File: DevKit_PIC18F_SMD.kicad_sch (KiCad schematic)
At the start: 25 parts, among them J1 PIC_ICSP_ICD, J2 USB_B_Mini, J5 RIGHT_PORT, J6 LEFT_PORT, SW1 SW_RST, X1 16MHz

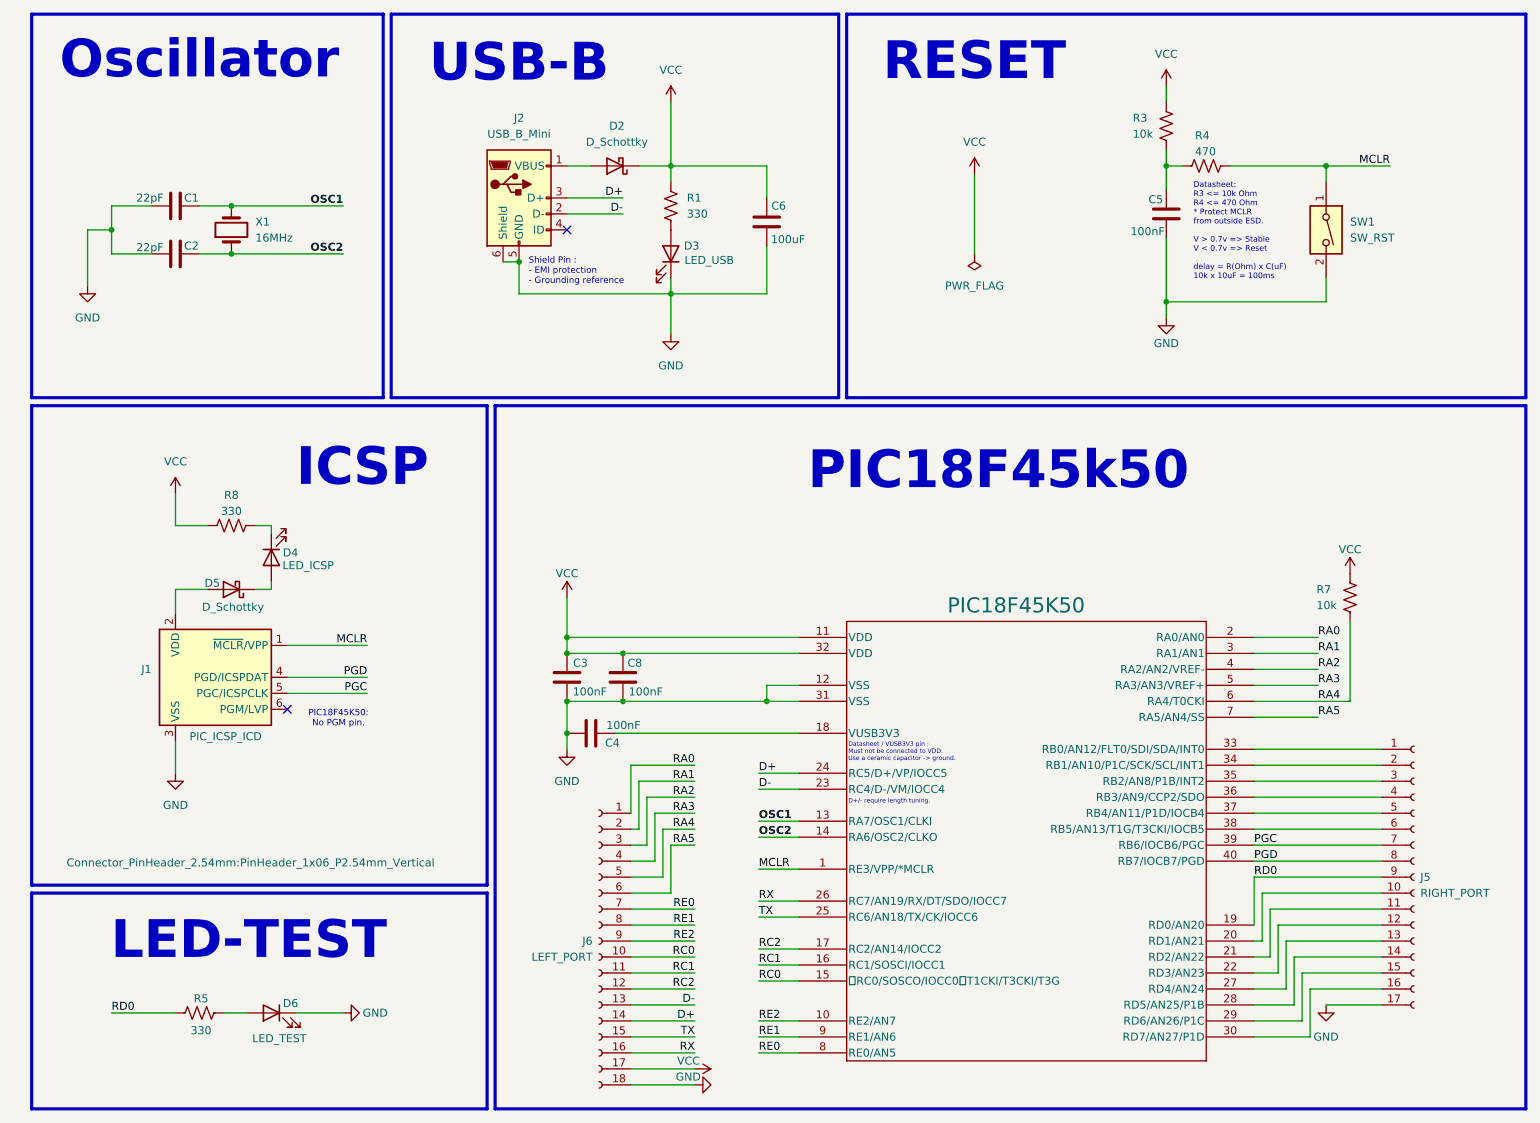
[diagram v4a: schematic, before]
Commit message: Rev.3 : refine part-selection for JLCPCB fabrication & silkscreen.
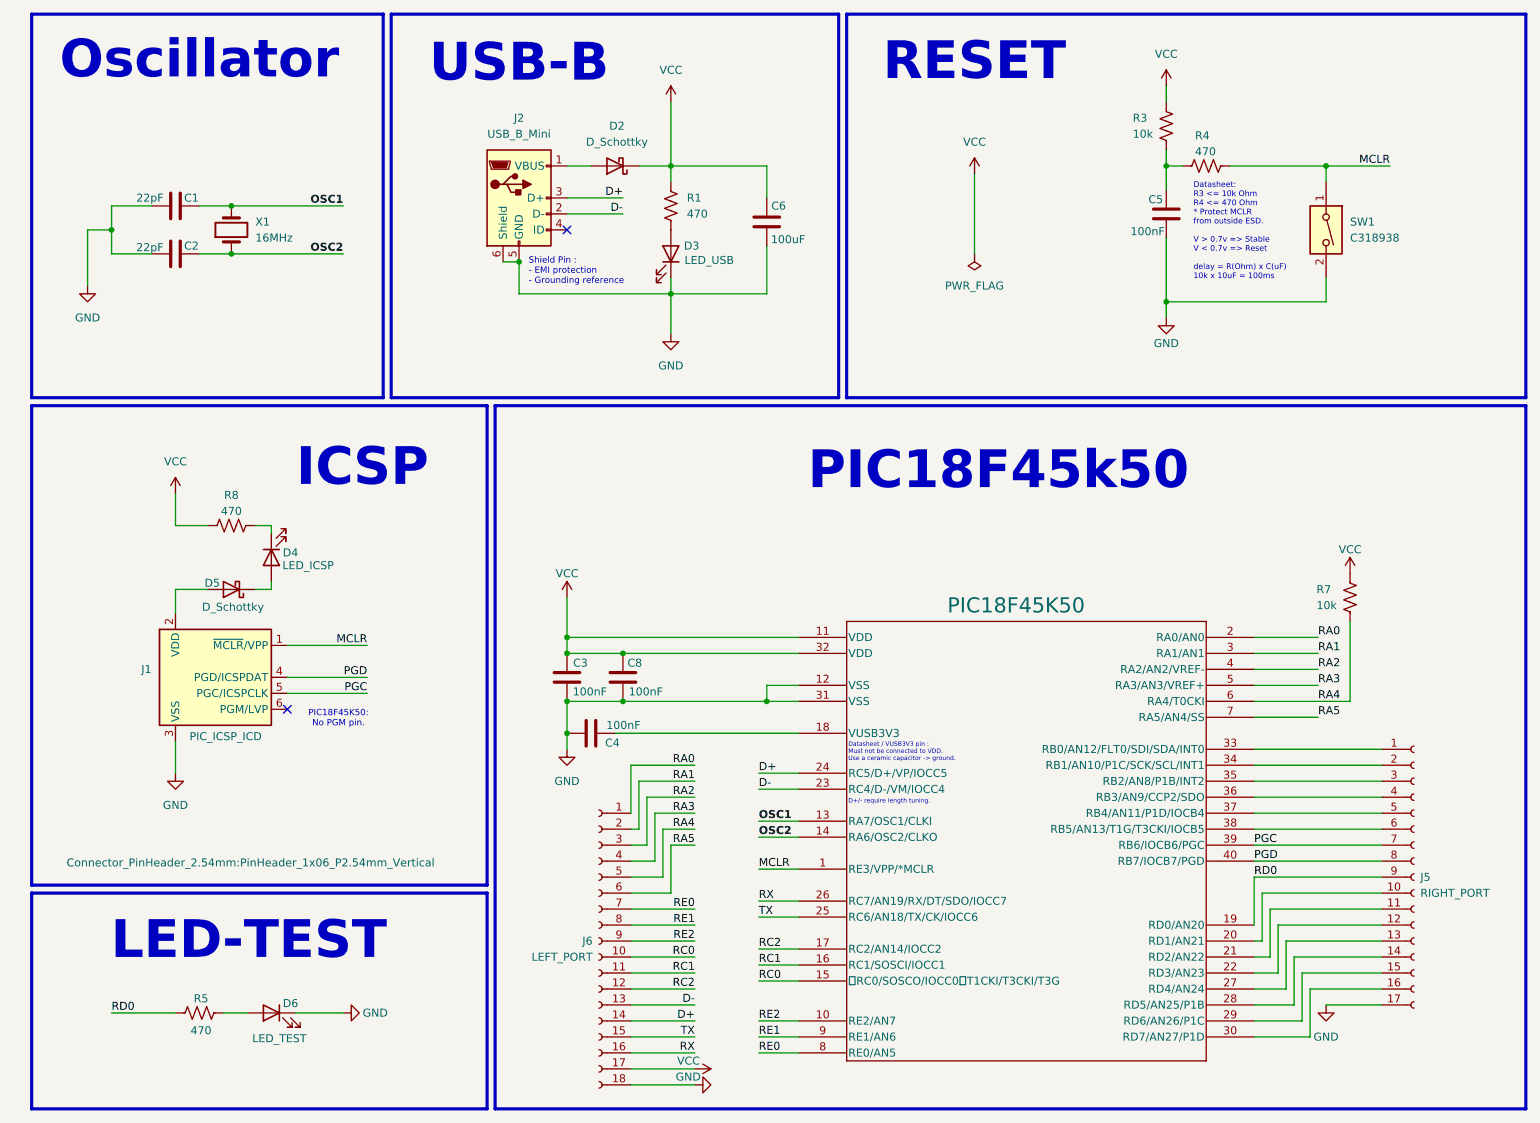
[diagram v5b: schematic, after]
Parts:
- C1, C2: footprint Capacitor_SMD:C_1206_3216Metric -> Capacitor_SMD:C_0805_2012Metric
- D3, D4, D6: footprint LED_SMD:LED_1206_3216Metric -> LED_SMD:LED_0805_2012Metric
- R1, R8: value 330 -> 470; footprint Resistor_SMD:R_1206_3216Metric -> Resistor_SMD:R_0805_2012Metric
- R4: footprint Resistor_SMD:R_1206_3216Metric -> Resistor_SMD:R_0805_2012Metric
- R5: value 330 -> 470
- SW1: value SW_RST -> C318938; footprint Button_Switch_SMD:SW_Push_SPST_NO_Alps_SKRK -> Button_Switch_SMD:SW_SPST_SKQG_WithStem
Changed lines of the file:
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@@
 			)
 		)
-		(property "Footprint" "LED_SMD:LED_1206_3216Metric"
+		(property "Footprint" "LED_SMD:LED_0805_2012Metric"
 			(at 112.776 50.8 0)
 			(effects
@@
 			)
 		)
-		(property "Value" "SW_RST"
+		(property "Value" "C318938"
 			(at 223.52 48.2599 90)
 			(effects
@@
 			)
 		)
-		(property "Footprint" "Button_Switch_SMD:SW_Push_SPST_NO_Alps_SKRK"
+		(property "Footprint" "Button_Switch_SMD:SW_SPST_SKQG_WithStem"
 			(at 219.71 46.99 0)
 			(effects
@@
 			)
 		)
-		(property "Value" "330"
+		(property "Value" "470"
 			(at 45.72 91.694 90)
 			(effects
@@
 			)
 		)
-		(property "Footprint" "Resistor_SMD:R_1206_3216Metric"
+		(property "Footprint" "Resistor_SMD:R_0805_2012Metric"
 			(at 45.974 92.964 90)
 			(effects
@@
 			)
 		)
-		(property "Value" "330"
+		(property "Value" "470"
 			(at 118.11 44.4499 0)
 			(effects
@@
 			)
 		)
-		(property "Footprint" "Resistor_SMD:R_1206_3216Metric"
+		(property "Footprint" "Resistor_SMD:R_0805_2012Metric"
 			(at 116.586 43.434 90)
 			(effects
@@
 			)
 		)
-		(property "Footprint" "LED_SMD:LED_1206_3216Metric"
+		(property "Footprint" "LED_SMD:LED_0805_2012Metric"
 			(at 52.07 171.45 0)
 			(effects
@@
 			)
 		)
-		(property "Footprint" "LED_SMD:LED_1206_3216Metric"
+		(property "Footprint" "LED_SMD:LED_0805_2012Metric"
 			(at 52.07 99.06 0)
 			(effects
@@
 			)
 		)
-		(property "Footprint" "Capacitor_SMD:C_1206_3216Metric"
+		(property "Footprint" "Capacitor_SMD:C_0805_2012Metric"
 			(at 33.02 42.2148 0)
 			(effects
@@
 			)
 		)
-		(property "Footprint" "Capacitor_SMD:C_1206_3216Metric"
+		(property "Footprint" "Capacitor_SMD:C_0805_2012Metric"
 			(at 33.02 49.8348 0)
 			(effects
@@
 			)
 		)
-		(property "Value" "330"
+		(property "Value" "470"
 			(at 40.894 174.244 90)
 			(effects
@@
 			)
 		)
-		(property "Footprint" "Resistor_SMD:R_1206_3216Metric"
+		(property "Footprint" "Resistor_SMD:R_0805_2012Metric"
 			(at 200.406 37.846 90)
 			(effects

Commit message: :Fix R5 size 1206 -> 0805 & BOM of D5,D2 -> C3758192
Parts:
- R5: footprint Resistor_SMD:R_1206_3216Metric -> Resistor_SMD:R_0805_2012Metric
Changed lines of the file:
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@@
 			)
 		)
-		(property "Footprint" "Resistor_SMD:R_1206_3216Metric"
+		(property "Footprint" "Resistor_SMD:R_0805_2012Metric"
 			(at 40.894 170.434 90)
 			(effects
